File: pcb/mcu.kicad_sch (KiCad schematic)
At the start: 23 parts, among them J1 XF2M-1415-1A, SW1 EVQ-Q2B02W, SW2 EVQ-Q2B02W, U1 ESP32-S3-WROOM-1-N8R2

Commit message: Fixed footprint for Buzzer, XFC, USB ESD, and Power Switcher
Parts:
- J1: footprint CRGM Connector:XF2C_1415-1A -> CRGM Connector:XF2M-1415-1A
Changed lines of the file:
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@@
 			)
 		)
-		(property "Footprint" "CRGM Connector:XF2C_1415-1A"
+		(property "Footprint" "CRGM Connector:XF2M-1415-1A"
 			(at 182.88 64.262 0)
 			(effects

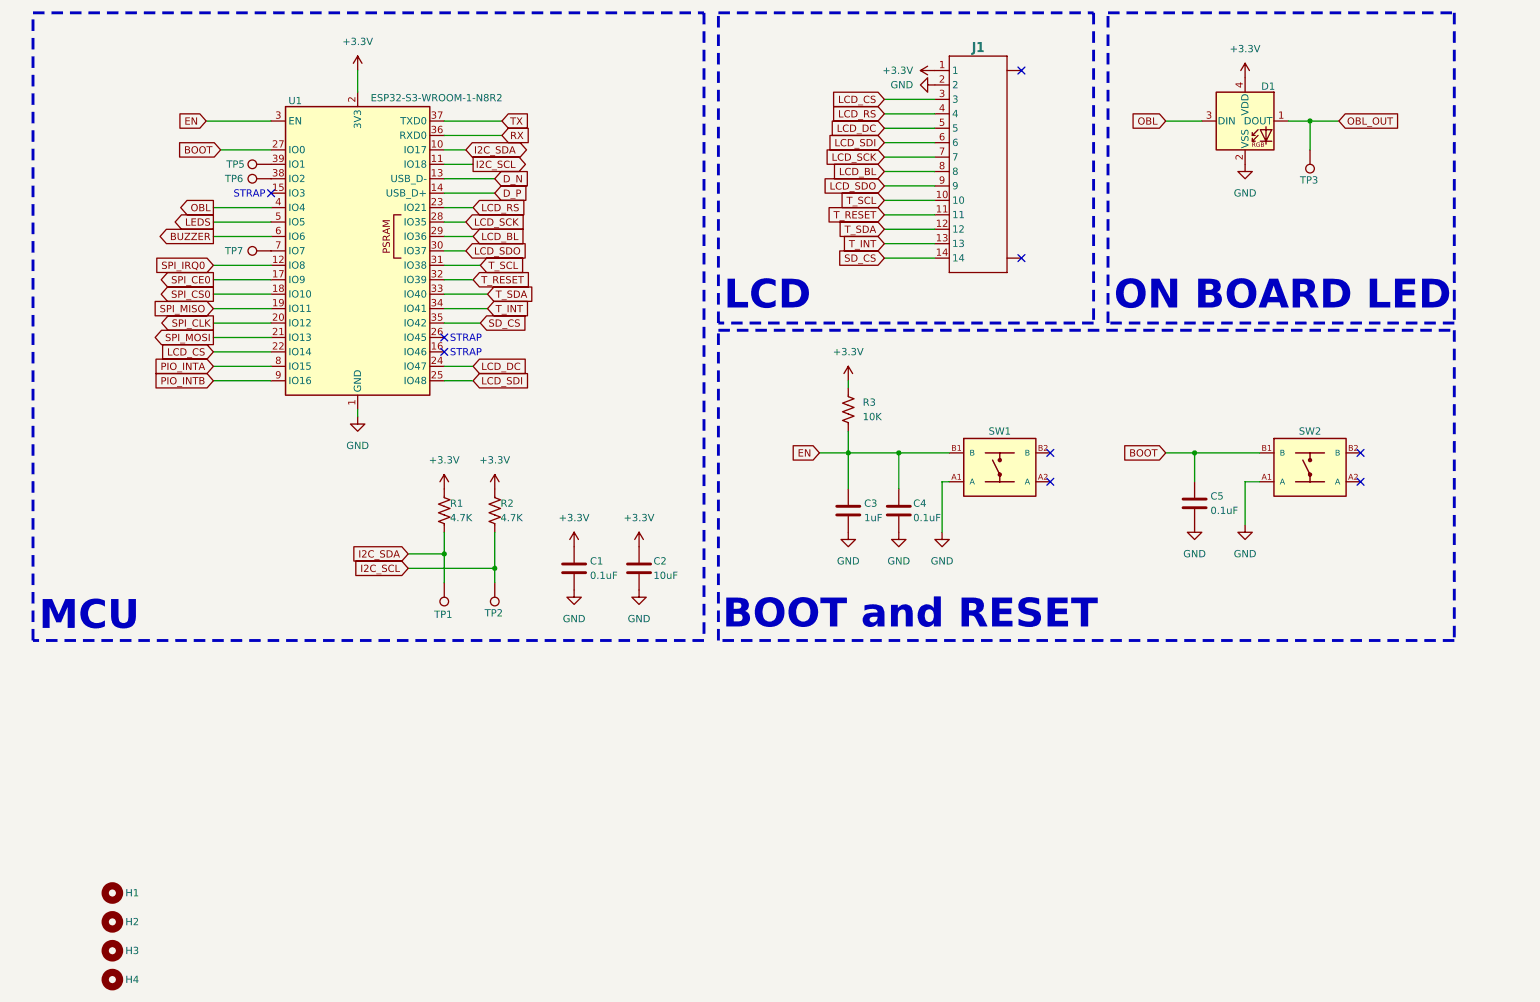
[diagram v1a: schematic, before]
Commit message: Added test points. Fixed license file.
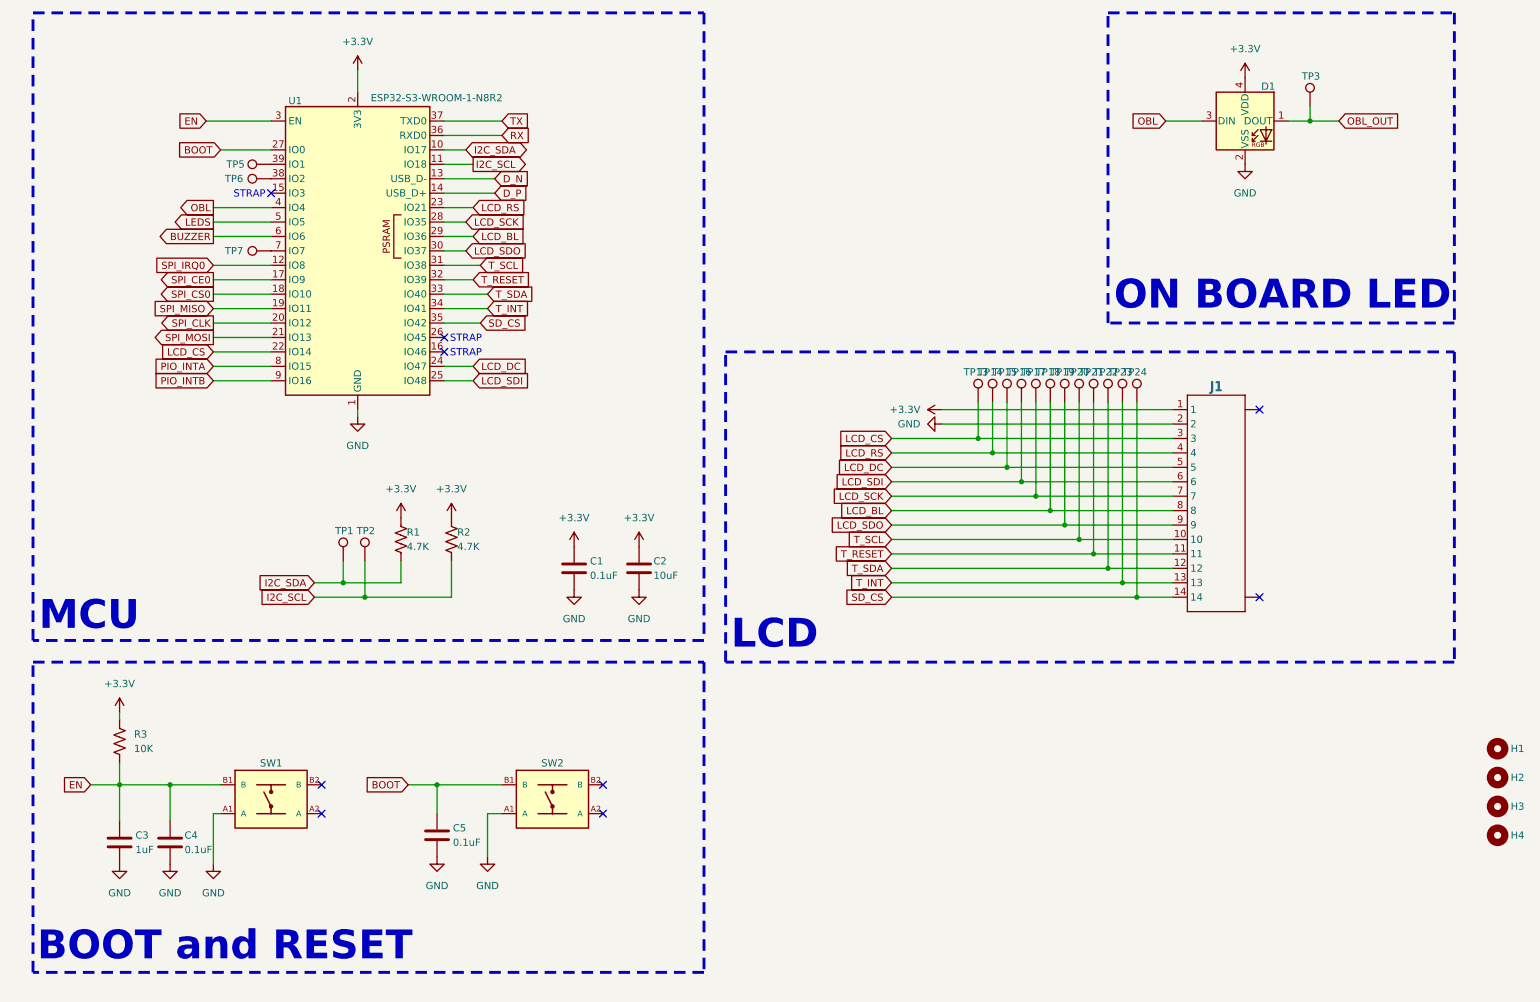
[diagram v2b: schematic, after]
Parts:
- added TP13, TP14, TP15, TP16, TP17, TP18, TP19, TP20, TP21, TP22, TP23, TP24: TP, CRGM Mechanical:TestPoint_Pad_D1.0mm, symbol Connector:TestPoint
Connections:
- net LCD_BL: now also TP18.1
- net LCD_CS: now also TP13.1
- net LCD_DC: now also TP15.1
- net LCD_RS: now also TP14.1
- net LCD_SCK: now also TP17.1
- net LCD_SDI: now also TP16.1
- net LCD_SDO: now also TP19.1
- net SD_CS: now also TP24.1
- net T_INT: now also TP23.1
- net T_RESET: now also TP21.1
- net T_SCL: now also TP20.1
- net T_SDA: now also TP22.1
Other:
- moved on the sheet: C3, C4, C5, H1, H2, H3, H4, J1, R1, R2, R3, SW1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

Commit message: Minor updates to ESP part number/footprint
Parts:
- U1: symbol RF_Module:ESP32-S3-WROOM-1 -> CRG Makes:ESP32-S3-WROOM-1-N8R2
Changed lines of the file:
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@@
 	)
 	(symbol
-		(lib_id "RF_Module:ESP32-S3-WROOM-1")
+		(lib_id "CRG Makes:ESP32-S3-WROOM-1-N8R2")
 		(at 73.66 58.42 0)
 		(unit 1)
@@
 		)
 		(property "Value" "ESP32-S3-WROOM-1-N8R2"
-			(at 75.946 31.496 0)
+			(at 88.392 31.75 0)
 			(effects
 				(font
 					(size 1.27 1.27)
 				)
-				(justify left)
 			)
 		)
 		(property "Footprint" "CRG Makes:ESP32-S3-WROOM-1-N8R2"
-			(at 73.66 55.88 0)
+			(at 73.66 97.536 0)
 			(effects
 				(font
@@
 		)
 		(property "Datasheet" "https://www.espressif.com/sites/default/files/documentation/esp32-s3-wroom-1_wroom-1u_datasheet_en.pdf"
-			(at 73.66 58.42 0)
+			(at 73.66 103.886 0)
 			(effects
 				(font
@@
 			)
 		)
-		(property "Description" "RF Module, ESP32-S3 SoC"
-			(at 73.66 58.42 0)
+		(property "Description" "RF Module, ESP32-S3 SoC, Wi-Fi 802.11b/g/n, Bluetooth, BLE, 32-bit, 3.3V, onboard antenna, SMD"
+			(at 73.66 101.854 0)
 			(effects
 				(font
@@
 		)
 		(property "Mouser" "356-ESP32-S3WRM1N8R2"
-			(at 73.66 58.42 0)
+			(at 73.66 110.49 0)
 			(effects
 				(font
@@
 		)
 		(property "Digikey" "5407-ESP32-S3-WROOM-1-N8R2-ND"
-			(at 73.66 58.42 0)
+			(at 73.66 108.204 0)
 			(effects
 				(font
@@
 		)
 		(property "LCSC" "C2913204"
-			(at 73.66 58.42 0)
+			(at 73.66 112.776 0)
 			(effects
 				(font

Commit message: Change name in schematic
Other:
- title: Node Hardware -> Hub Hardware
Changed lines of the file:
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@@
 	(paper "A4")
 	(title_block
-		(title "Node Hardware")
+		(title "Hub Hardware")
 		(date "<<release-date>>")
 		(rev "<<tag>>")

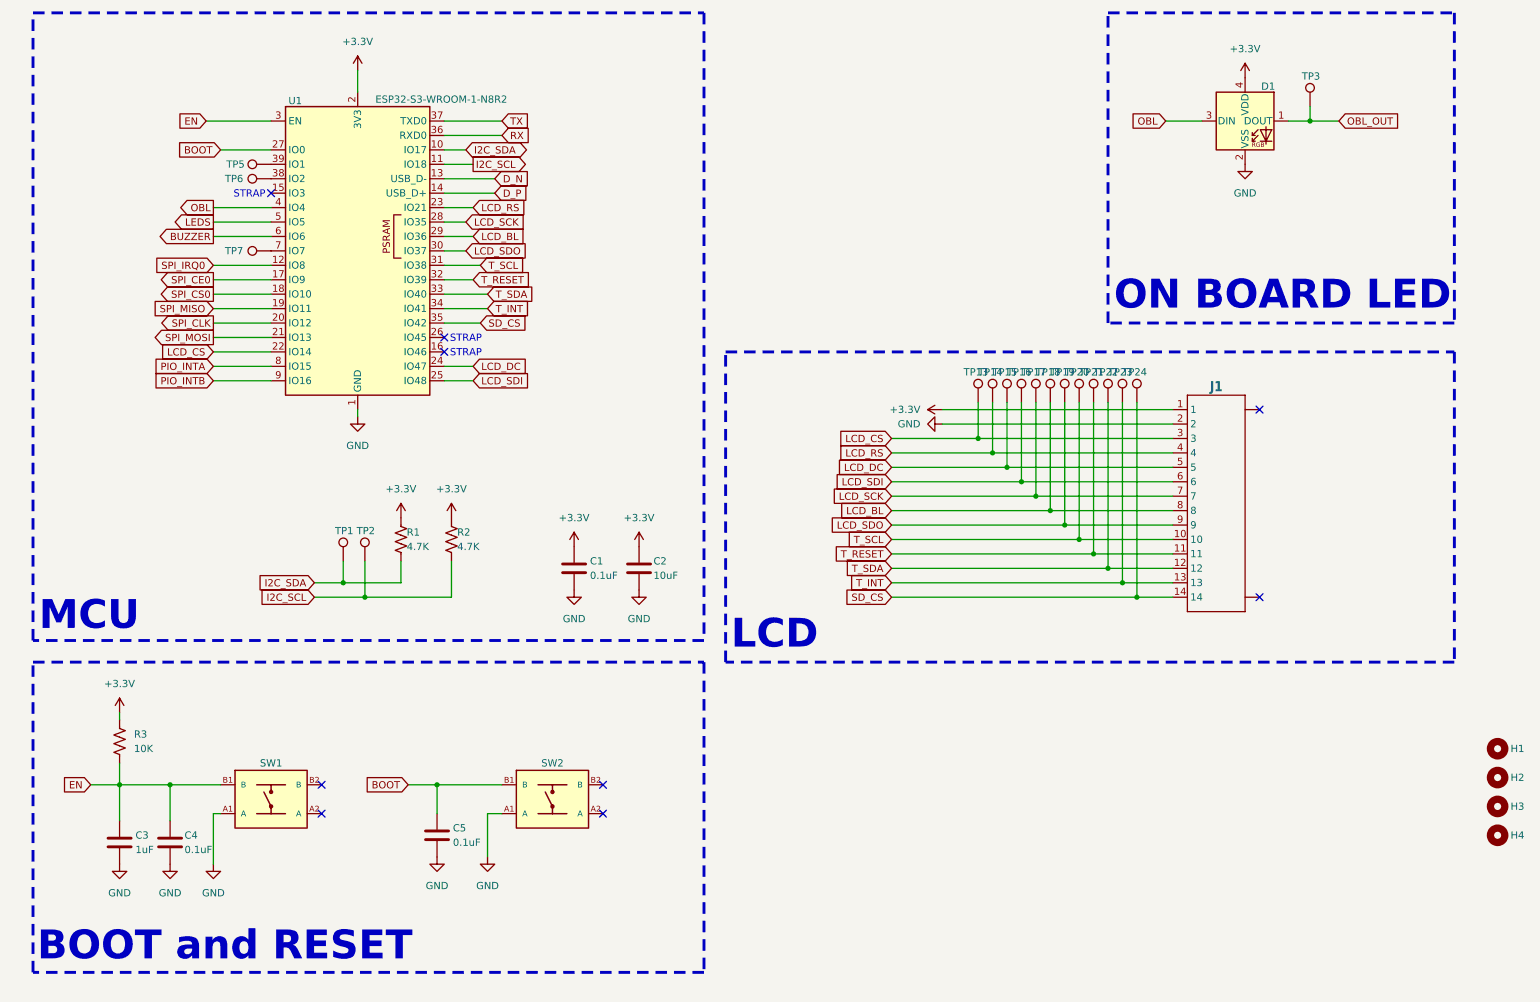
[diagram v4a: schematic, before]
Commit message: Renamed files; update with more test points
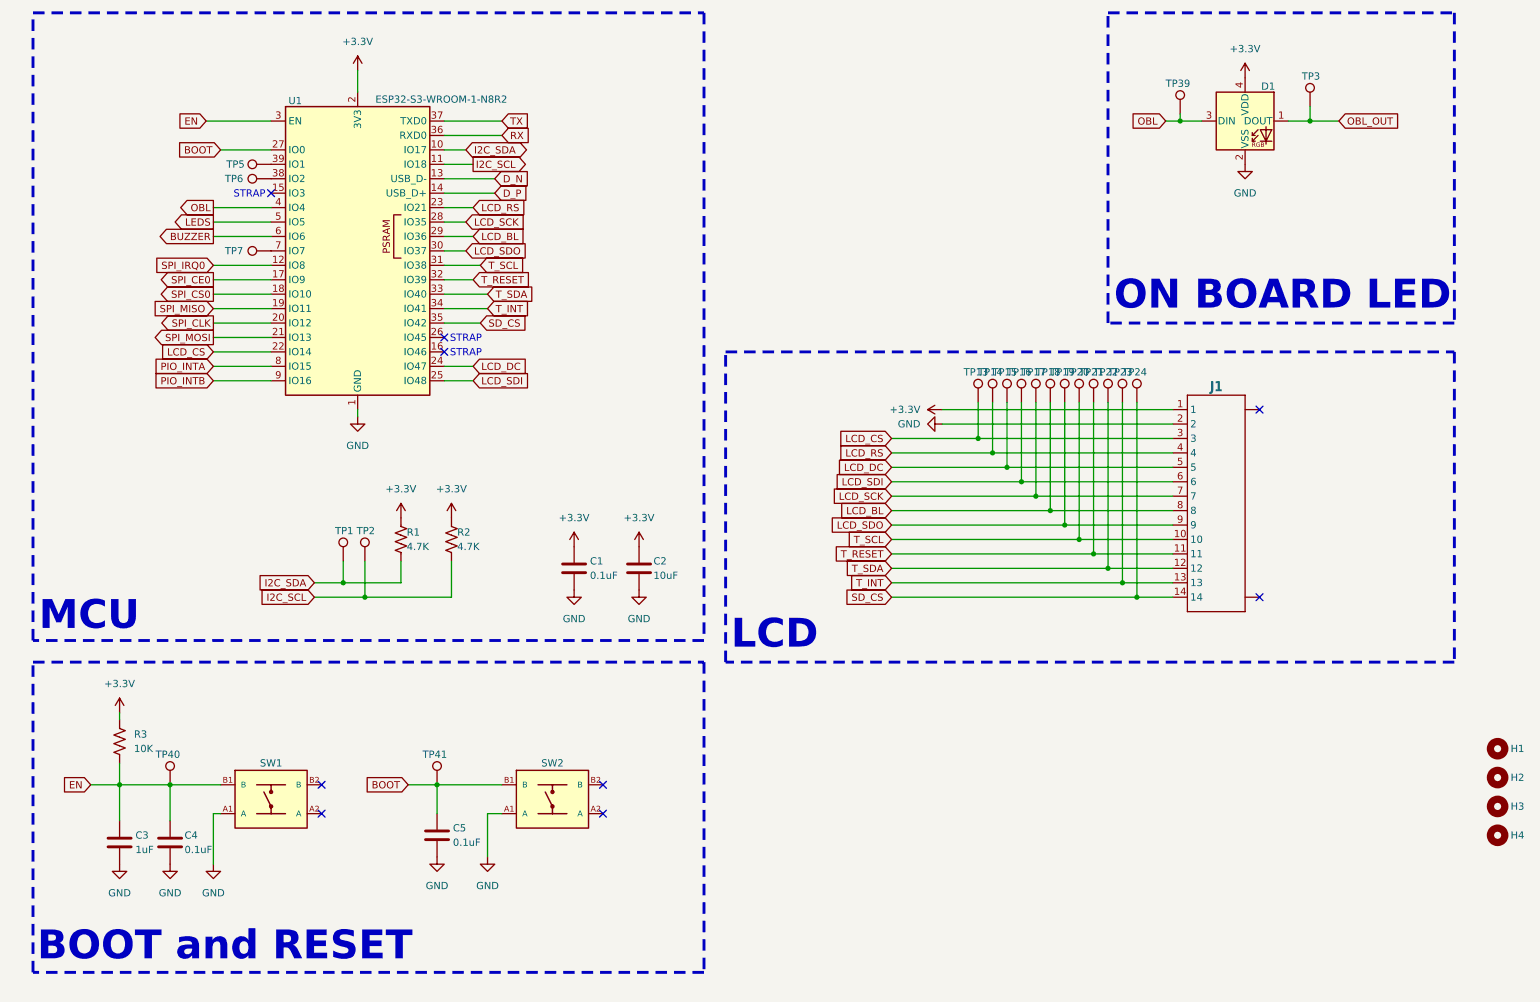
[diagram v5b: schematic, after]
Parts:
- added TP39, TP40, TP41: ~, CRGM Mechanical:TestPoint_Pad_D1.0mm, symbol Connector:TestPoint
- TP3: value TP -> ~
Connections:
- net BOOT: now also TP41.1
- net EN: now also TP40.1
- net OBL: now also TP39.1

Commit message: Renamed peripherals to interfaces; added test points; added led jumper
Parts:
- H1, H2, H3, H4: value MountingHole_Pad -> ~
- TP1, TP13, TP14, TP15, TP16, TP17, TP18, TP19, TP2, TP20, TP21, TP22, TP23, TP24, TP5, TP6, TP7: value TP -> ~
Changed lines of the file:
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@@
 			)
 		)
-		(property "Value" "TP"
+		(property "Value" "~"
 			(at 208.28 77.978 0)
 			(effects
@@
 			)
 		)
-		(property "Value" "TP"
+		(property "Value" "~"
 			(at 198.12 77.978 0)
 			(effects
@@
 			)
 		)
-		(property "Value" "TP"
+		(property "Value" "~"
 			(at 195.58 77.978 0)
 			(effects
@@
 			)
 		)
-		(property "Value" "TP"
+		(property "Value" "~"
 			(at 203.2 77.978 0)
 			(effects
@@
 			)
 		)
-		(property "Value" "MountingHole_Pad"
+		(property "Value" "~"
 			(at 270.002 151.384 0)
 			(effects
@@
 			)
 		)
-		(property "Value" "TP"
+		(property "Value" "~"
 			(at 193.04 77.978 0)
 			(effects
@@
 			)
 		)
-		(property "Value" "TP"
+		(property "Value" "~"
 			(at 72.898 105.664 0)
 			(effects
@@
 			)
 		)
-		(property "Value" "TP"
+		(property "Value" "~"
 			(at 190.5 77.978 0)
 			(effects
@@
 			)
 		)
-		(property "Value" "MountingHole_Pad"
+		(property "Value" "~"
 			(at 273.304 158.496 0)
 			(effects
@@
 			)
 		)
-		(property "Value" "TP"
+		(property "Value" "~"
 			(at 46.99 58.42 90)
 			(effects
@@
 			)
 		)
-		(property "Value" "MountingHole_Pad"
+		(property "Value" "~"
 			(at 273.558 161.544 0)
 			(effects
@@
 			)
 		)
-		(property "Value" "TP"
+		(property "Value" "~"
 			(at 213.36 77.978 0)
 			(effects
@@
 			)
 		)
-		(property "Value" "TP"
+		(property "Value" "~"
 			(at 185.42 77.978 0)
 			(effects
@@
 			)
 		)
-		(property "Value" "TP"
+		(property "Value" "~"
 			(at 76.708 105.664 0)
 			(effects
@@
 			)
 		)
-		(property "Value" "TP"
+		(property "Value" "~"
 			(at 210.82 77.978 0)
 			(effects
@@
 			)
 		)
-		(property "Value" "MountingHole_Pad"
+		(property "Value" "~"
 			(at 276.606 168.656 0)
 			(effects
@@
 			)
 		)
-		(property "Value" "TP"
+		(property "Value" "~"
 			(at 187.96 77.978 0)
 			(effects
@@
 			)
 		)
-		(property "Value" "TP"
+		(property "Value" "~"
 			(at 200.66 77.978 0)
 			(effects
@@
 			)
 		)
-		(property "Value" "TP"
+		(property "Value" "~"
 			(at 46.736 43.18 90)
 			(effects
@@
 			)
 		)
-		(property "Value" "TP"
+		(property "Value" "~"
 			(at 205.74 77.978 0)
 			(effects
@@
 			)
 		)
-		(property "Value" "TP"
+		(property "Value" "~"
 			(at 46.736 45.72 90)
 			(effects

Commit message: Adjusting for consistency
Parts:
- removed H1, H2, H3, H4: ~, CRGM Mechanical:MountingHole_3.2mm_M3_Pad_Via, symbol Mechanical:MountingHole
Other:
- title: Hub Hardware -> Aquarius Hub
- moved on the sheet: D1, J1, TP13, TP14, TP15, TP16, TP17, TP18, TP19, TP20, TP21, TP22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
